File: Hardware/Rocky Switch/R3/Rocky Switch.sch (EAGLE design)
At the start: 18 parts, among them T1 2SC1815, T2 2SC1815, T3 C1815

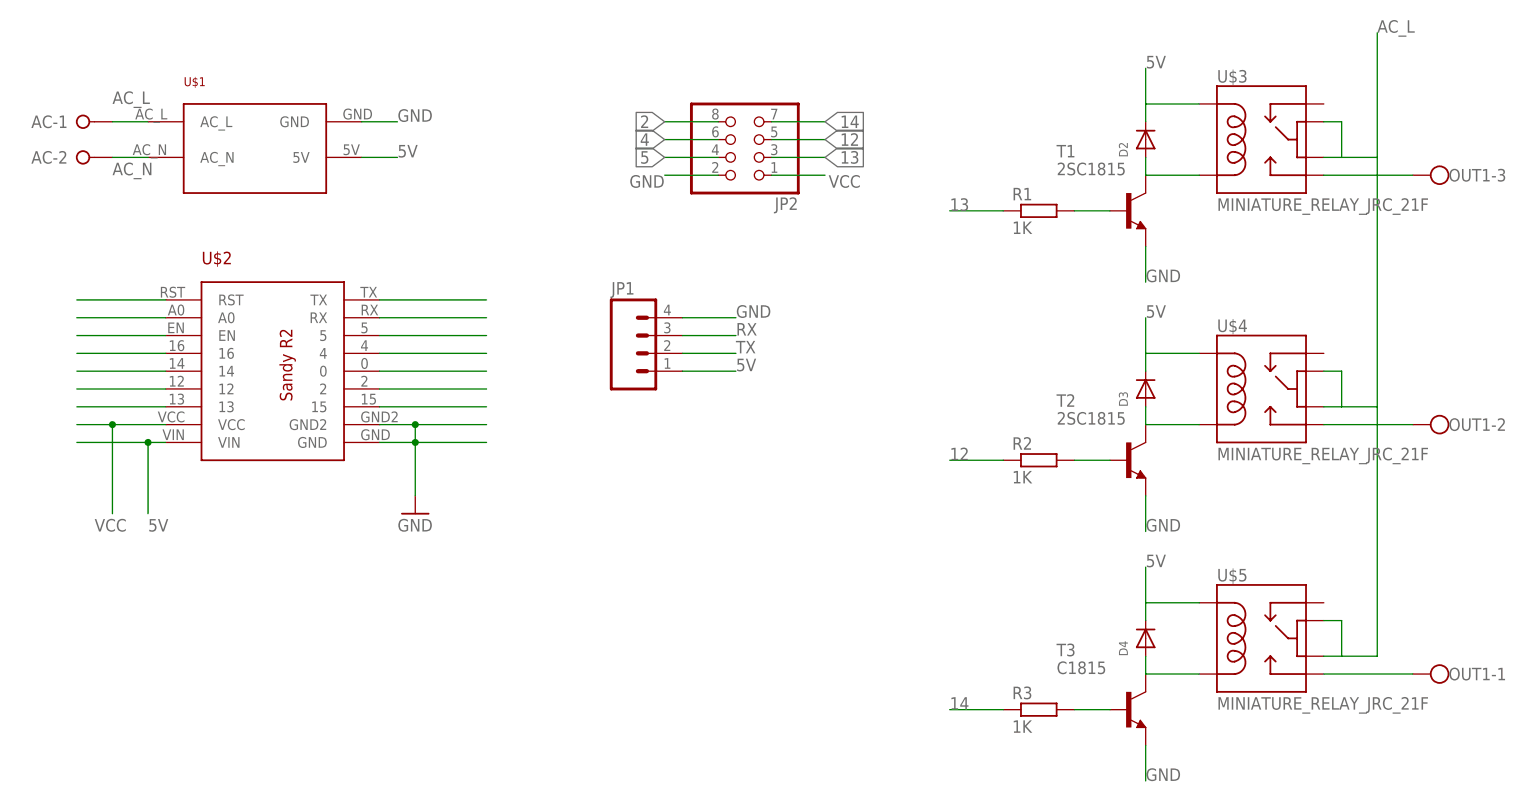
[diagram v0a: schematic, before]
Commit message: Rename SwitchNode to Rocky Switch and change to use Wemos D1 Mini
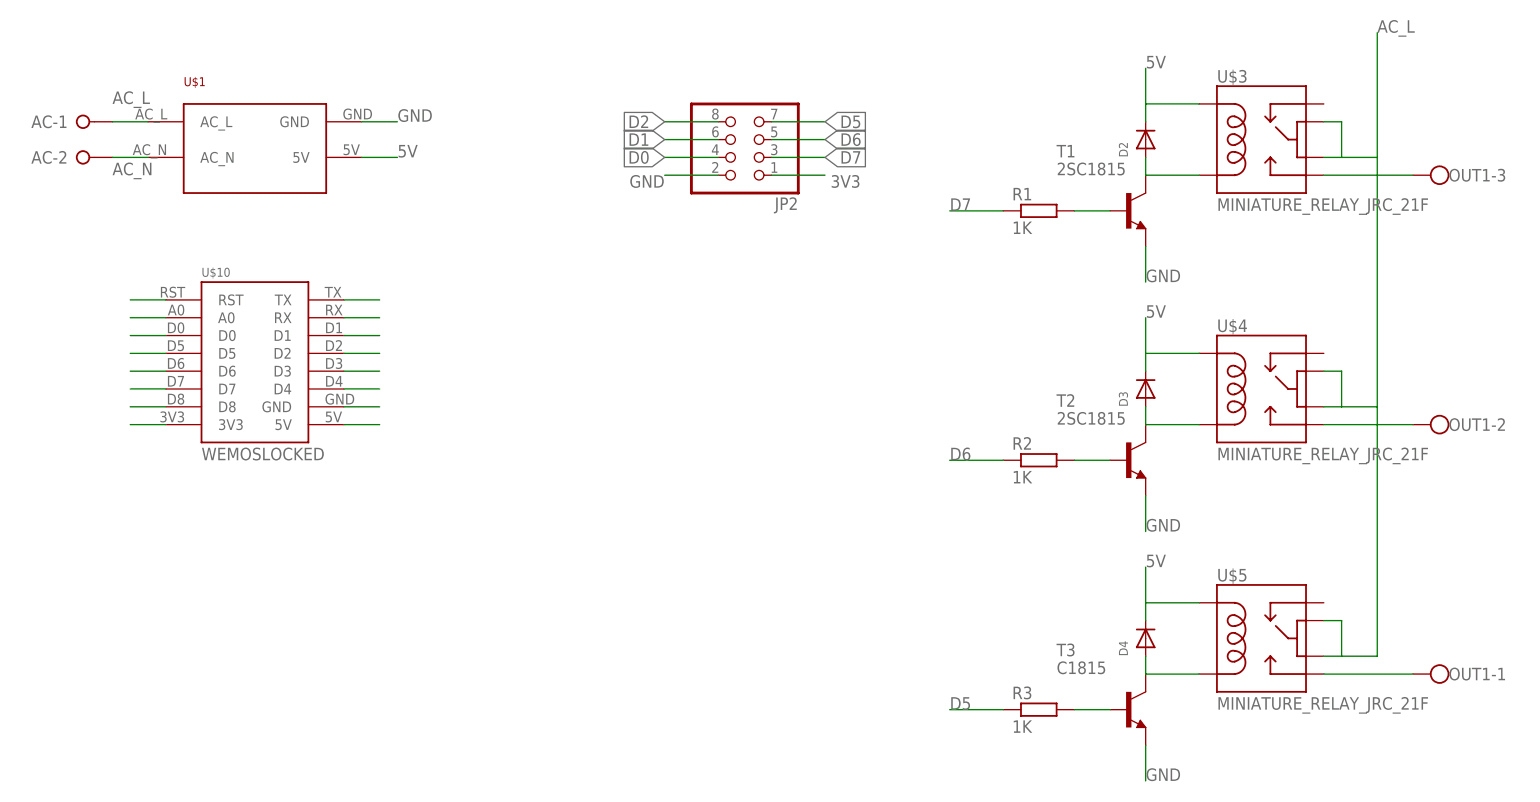
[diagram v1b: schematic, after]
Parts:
- removed JP1: (no value), SparkFun-Connectors:M04PTH
- removed U$2: MINI-ESP, My Eagle Lib:MINI-ESP
- added U$10: WEMOSLOCKED, My Eagle Lib:WEMOSLOCKED
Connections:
- removed net 0: U$2.0
- removed net 12: JP2.5, R2.1, U$2.12
- removed net 13: JP2.3, R1.1, U$2.13
- removed net 14: JP2.7, R3.1, U$2.14
- removed net 16: U$2.16
- removed net 2: JP2.8, U$2.2
- removed net 4: JP2.6, U$2.4
- removed net 5: JP2.4, U$2.5
- removed net EN: U$2.EN
- removed net RST: U$2.RST
- removed net VCC: JP2.1, U$2.VCC
- new net 3V3: JP2.1, U$10.3V3
- new net D0: JP2.4, U$10.D0
- new net D1: JP2.6, U$10.D1
- new net D2: JP2.8, U$10.D2
- new net D3: U$10.D3
- new net D4: U$10.D4
- new net D5: JP2.7, R3.1, U$10.D5
- new net D6: JP2.5, R2.1, U$10.D6
- new net D7: JP2.3, R1.1, U$10.D7
- new net RST1: U$10.RST
- net 5V: now also U$10.5V; no longer JP1.1, U$2.VIN
- net A0: now also U$10.A0; no longer U$2.A0
- net D8: now also U$10.D8; no longer U$2.15
- net GND: now also U$10.GND; no longer JP1.4, U$2.GND, U$2.GND2
- net RX: now also U$10.RX; no longer JP1.3, U$2.RX
- net TX: now also U$10.TX; no longer JP1.2, U$2.TX
